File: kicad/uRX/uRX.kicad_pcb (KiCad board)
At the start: 2 copper layers, 13 x 1.4 mm, 134 parts, among them J1 RF_AM_GND, J2 C165948, J3 AudioJack2_Ground, J4 +5Vfiltered, J5 +5V, J5 Bat, J5 GND, J6 U.FL, J7 +3.3Vfiltered, J9 RF_AM__In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

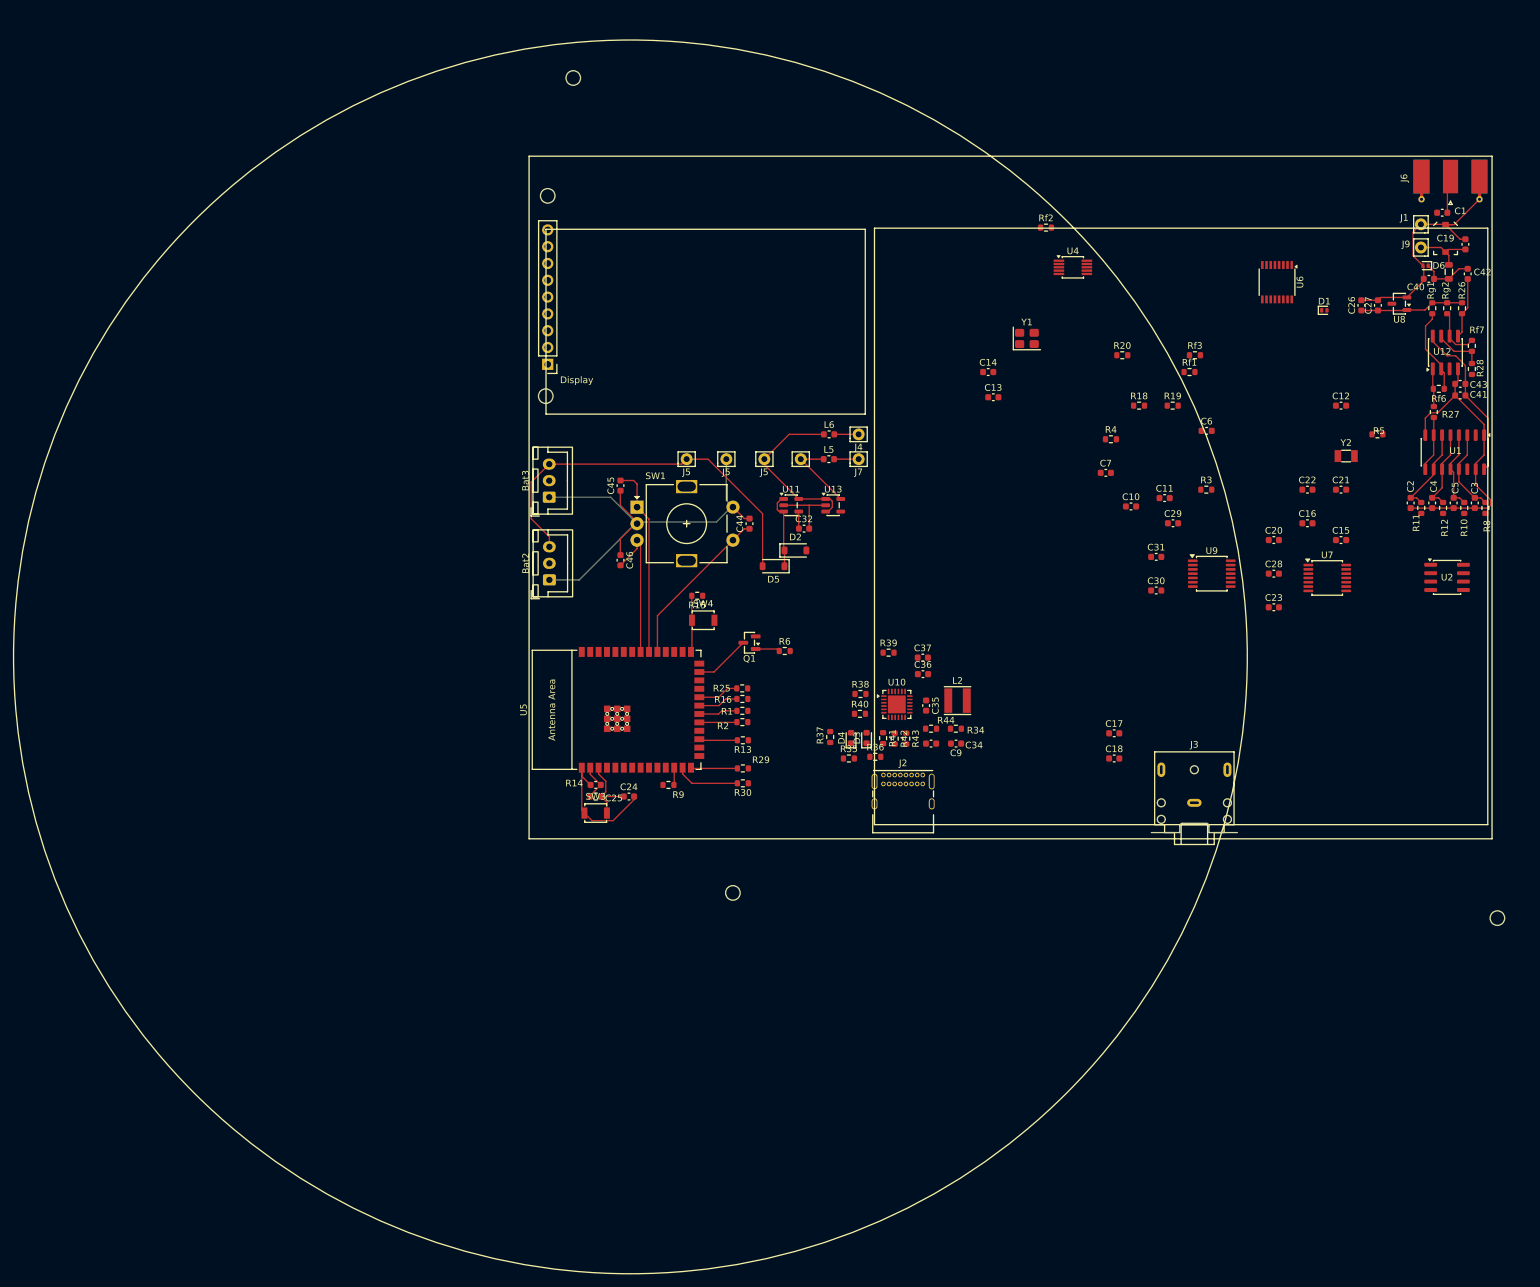
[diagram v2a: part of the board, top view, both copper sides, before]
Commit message: work on rf part pcb
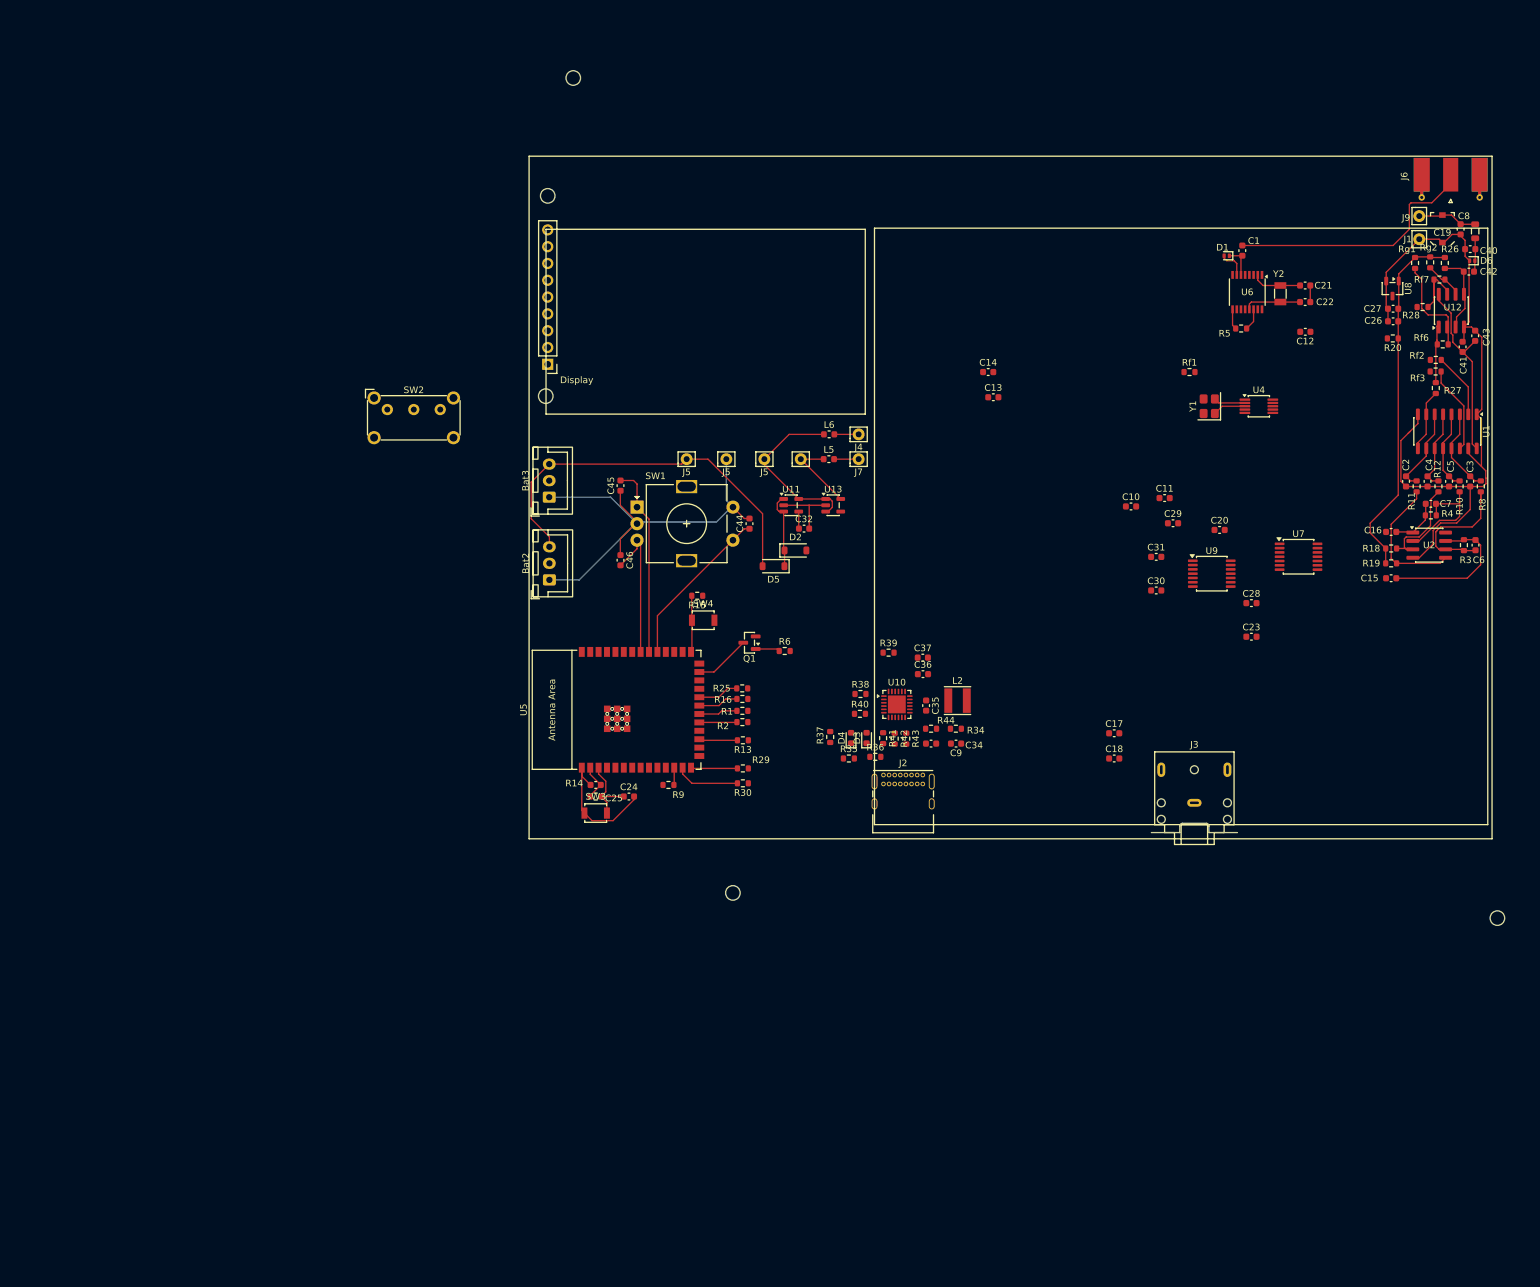
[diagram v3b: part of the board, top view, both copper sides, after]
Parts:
- added SW2: SW_DPDT_x2, Button_Switch_THT:SW_E-Switch_EG1224_SPDT_Angled, F.Cu at (58.2, 74.2)
- moved Rf2 62.2 mm to (216.8, 66.8), turned to 180 degrees
- moved R4 49.7 mm to (216.0, 90.2)
- moved C7 49.4 mm to (216.0, 88.5), turned to 180 degrees
- moved C6 44.2 mm to (222.8, 94.8), turned to 90 degrees
- moved R18 43.8 mm to (210.0, 95.2), turned to 180 degrees
- moved R20 41.0 mm to (210.2, 63.5), turned to 180 degrees
- moved R19 40.7 mm to (210.0, 97.5), turned to 180 degrees
- moved R3 39.8 mm to (221.0, 94.8), turned to -90 degrees
- moved Rf3 36.5 mm to (216.7, 68.5), turned to 180 degrees
- moved U4 35.1 mm to (190.0, 73.8)
- moved C21 31.3 mm to (197.0, 55.5), turned to 180 degrees
- moved C1 30.8 mm to (187.5, 50.2), turned to 90 degrees
- moved Y1 29.4 mm to (182.5, 73.8), turned to 90 degrees
- moved C22 28.4 mm to (197.0, 58.0), turned to 180 degrees
- moved Y2 26.5 mm to (193.2, 56.8), turned to 90 degrees
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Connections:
- U11 pad 5: +5V -> Net-(SW2A-A)
- U2 pad 4: (no net) -> GND
- U2 pad 8: (no net) -> +5Vfiltered
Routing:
- net /VRev2.5: track 15.7 -> 54.6 mm
- net Net-(J6-In): track 5.67 -> 38.9 mm
- net GND: track 181.3 -> 213.2 mm
- net Net-(C15-Pad1): track 0.00 -> 22.3 mm
- net Net-(U2B--): track 0.00 -> 21.6 mm
- net Net-(U2B-+): track 0.00 -> 20.5 mm
- net Net-(U2A--): track 0.00 -> 17.7 mm
- net Net-(U2A-+): track 0.00 -> 15.6 mm
- net Net-(U1-S0): track 0.00 -> 13.3 mm
- net Net-(U1-S1): track 0.00 -> 9.92 mm
- net Net-(U6-RCLK): track 0.00 -> 8.58 mm
- net Net-(C16-Pad1): track 0.00 -> 7.69 mm
- net Net-(U6-DClk): track 0.00 -> 7.52 mm
- net Net-(U4-XB): track 0.00 -> 4.99 mm
- net Net-(D1-K): track 0.00 -> 4.93 mm
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
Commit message: finalize rf, 4732 and clock
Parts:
- removed Rf2, Rf3: 47, Resistor_SMD:R_0603_1608Metric
- removed Y1: 25MHz, Crystal:Crystal_SMD_3225-4Pin_3.2x2.5mm
- added +3.3V: +3.3V, TestPoint:TestPoint_THTPad_1.0x1.0mm_Drill0.5mm, F.Cu at (130.0, 86.0)
- added 2211Out1: TestPoint, TestPoint:TestPoint_THTPad_1.0x1.0mm_Drill0.5mm, F.Cu at (205.0, 66.3)
- added C33: 10n, Capacitor_SMD:C_0603_1608Metric, F.Cu at (184.0, 75.0)
- added C38: 10n, Capacitor_SMD:C_0603_1608Metric, F.Cu at (184.0, 73.3)
- added CLK0: CLK0, TestPoint:TestPoint_THTPad_1.0x1.0mm_Drill0.5mm, F.Cu at (190.0, 78.0)
- added CLK1: CLK1, TestPoint:TestPoint_THTPad_1.0x1.0mm_Drill0.5mm, F.Cu at (190.0, 70.5)
- added CLK2: CLK2, TestPoint:TestPoint_THTPad_1.0x1.0mm_Drill0.5mm, F.Cu at (190.0, 81.8)
- added GND1: TestPoint_2Pole, TestPoint:TestPoint_2Pads_Pitch2.54mm_Drill0.8mm, F.Cu at (81.8, 107.5)
- added Rf4: 47, Resistor_SMD:R_0603_1608Metric, F.Cu at (201.0, 75.0)
- added Rf5: 47, Resistor_SMD:R_0603_1608Metric, F.Cu at (204.0, 73.2)
- added TP3: VRef, TestPoint:TestPoint_THTPad_1.0x1.0mm_Drill0.5mm, F.Cu at (221.8, 89.0)
- added TP8: +5V, TestPoint:TestPoint_THTPad_1.0x1.0mm_Drill0.5mm, F.Cu at (130.0, 90.5)
- added VBatt: VBatt, TestPoint:TestPoint_THTPad_1.0x1.0mm_Drill0.5mm, F.Cu at (99.8, 80.8)
- added X1: X322525MOB4SI, Crystal:Crystal_SMD_3225-4Pin_3.2x2.5mm, F.Cu at (172.7, 74.8)
- C13, C14: value 2..20p -> 100n
- Rf1: value 33 -> 47
- moved C14 35.8 mm to (184.0, 76.8)
- moved C13 27.1 mm to (176.9, 72.8)
- moved R19 16.9 mm to (220.8, 84.5), turned to 0 degrees
- moved C2 15.7 mm to (216.2, 70.0), turned to 0 degrees
- moved R11 14.7 mm to (217.1, 71.5), turned to 180 degrees
- moved C1 14.4 mm to (201.2, 54.6)
- moved D1 14.4 mm to (198.9, 55.4)
- moved R18 14.0 mm to (220.8, 86.2), turned to 0 degrees
- moved C12 13.4 mm to (210.2, 60.5)
- moved C6 13.2 mm to (216.9, 82.8), turned to 180 degrees
- moved R5 12.6 mm to (195.4, 52.4), turned to 0 degrees
- moved U7 12.3 mm to (193.5, 108.5)
- moved C4 12.1 mm to (216.2, 73.0), turned to 0 degrees
- moved Rf1 12.0 mm to (184.0, 79.8), turned to 180 degrees
- moved U4 11.8 mm to (178.5, 76.0)
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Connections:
- C13 pad 1: Net-(U4-XA) -> +3.3V
- C14 pad 1: Net-(U4-XB) -> +3.3V
- U2 pad 4: GND -> (no net)
- U2 pad 8: +5Vfiltered -> (no net)
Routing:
- net GND: track 213.2 -> 156.1 mm, vias 12 -> 16
- net /VRev2.5: track 54.6 -> 79.7 mm
- net Net-(C38-Pad2): track 0.00 -> 21.2 mm
- net Net-(C33-Pad2): track 0.00 -> 18.4 mm
- net +5Vfiltered: track 29.5 -> 14.5 mm
- net Net-(U2B--): track 21.6 -> 8.09 mm
- net Net-(U6-AMI): track 0.00 -> 12.8 mm
- net Net-(J6-In): track 38.9 -> 27.0 mm
- net +3.3V: track 17.7 -> 26.7 mm
- net Net-(U1-S0): track 13.3 -> 5.80 mm
- net Net-(R28-Pad2): track 11.9 -> 5.32 mm
- net Net-(U4-CLK1): track 0.00 -> 6.07 mm
- net ADC_SCKI: track 0.00 -> 6.00 mm
- net +5V: track 26.3 -> 32.1 mm
- net Net-(U4-CLK2): track 0.00 -> 4.35 mm
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
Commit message: connect all together, v0
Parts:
- removed +3.3V: +3.3V, TestPoint:TestPoint_THTPad_1.0x1.0mm_Drill0.5mm
- removed J4: +5Vfiltered, Connector_Pin:Pin_D0.9mm_L10.0mm_W2.4mm_FlatFork
- removed J7: +3.3Vfiltered, Connector_Pin:Pin_D0.9mm_L10.0mm_W2.4mm_FlatFork
- removed TP8: +5V, TestPoint:TestPoint_THTPad_1.0x1.0mm_Drill0.5mm
- removed VBatt: VBatt, TestPoint:TestPoint_THTPad_1.0x1.0mm_Drill0.5mm
- added J10: GPIO_A, Connector_PinHeader_2.54mm:PinHeader_1x12_P2.54mm_Vertical, F.Cu at (130.0, 108.2)
- moved C18 64.3 mm to (179.5, 63.8)
- moved C10 62.8 mm to (223.0, 68.2), turned to -90 degrees
- moved C17 62.0 mm to (184.8, 63.5)
- moved C11 56.1 mm to (221.0, 68.2), turned to -90 degrees
- moved C23 25.1 mm to (182.3, 94.2)
- moved C30 24.7 mm to (168.5, 87.5)
- moved C28 22.6 mm to (181.5, 91.8), turned to 90 degrees
- moved C31 22.3 mm to (167.8, 85.0), turned to 90 degrees
- moved C29 19.0 mm to (165.9, 84.9), turned to 90 degrees
- moved U7 15.8 mm to (188.8, 93.5)
- moved C20 11.3 mm to (179.0, 91.8), turned to 90 degrees
- moved R37 8.99 mm to (129.8, 116.0), turned to 0 degrees
- moved U9 6.76 mm to (174.5, 86.0)
- moved R39 5.37 mm to (129.8, 114.2), turned to 180 degrees
- moved D3 5.20 mm to (125.5, 124.0)
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- renumbered CLK0 to TP4, CLK1 to TP5, CLK2 to TP6, TP3 to VRef1
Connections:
- C29 pad 2: +5Vfiltered -> +5V
- C30 pad 2: +3.3Vfiltered -> +3.3V
- C31 pad 2: +5Vfiltered -> +5V
- R5 pad 1: +3.3Vfiltered -> +3.3V
- U10 pad 15: Net-(U10-LX-Pad15) -> Net-(C35-Pad1)
- U10 pad 17: Net-(U10-LX-Pad15) -> Net-(C35-Pad1)
- U5 pad 23: unconnected-(U5-GPIO21-Pad23) -> RST_4732
- U5 pad 7: RST_4732 -> unconnected-(U5-GPIO7/TOUCH7/ADC1_CH6-Pad7)
- U6 pad 14: +3.3Vfiltered -> +3.3V
- U9 pad 1: +5Vfiltered -> +5V
- U9 pad 3: +5Vfiltered -> +5V
- U9 pad 4: +3.3Vfiltered -> +3.3V
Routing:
- net Net-(Bat2-Pin_2): track 0.00 -> 85.8 mm
- net GND: track 156.1 -> 239.2 mm, vias 16 -> 18
- net VBUS: track 0.00 -> 36.1 mm
- net ADC_SCKI: track 6.00 -> 40.8 mm
- net Net-(U9-VINL): track 0.00 -> 27.5 mm
- net +VBatt: track 62.8 -> 89.8 mm
- net Net-(U9-VINR): track 0.00 -> 23.3 mm
- net Net-(U7-VINL): track 0.00 -> 20.5 mm
- net Net-(D3-A): track 0.00 -> 19.3 mm
- net Net-(U7-VINR): track 0.00 -> 19.3 mm
- net Net-(U6-ROut): track 0.00 -> 17.8 mm
- net +5Vfiltered: track 14.5 -> 28.5 mm
- net Net-(J2-CC2): track 0.00 -> 13.5 mm
- net Net-(J2-SHIELD): track 0.00 -> 9.83 mm
- net Net-(C35-Pad1): track 0.00 -> 8.82 mm
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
